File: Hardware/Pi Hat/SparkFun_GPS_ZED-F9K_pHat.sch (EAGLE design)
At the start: 67 parts, among them J1 QWIIC_RIGHT_ANGLE, J2 RASPBERRYPI-40-PIN-GPIO_SMD_S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, J4 U.FL, U1 UBLOX_ZED_F9R

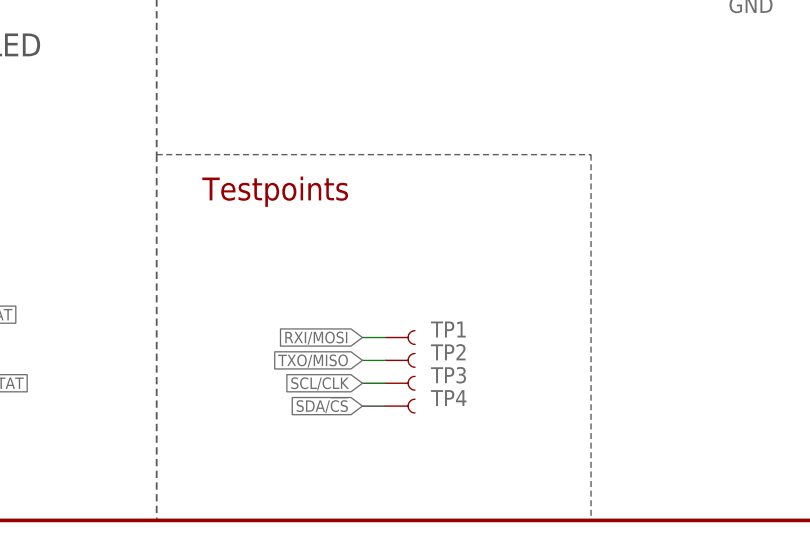
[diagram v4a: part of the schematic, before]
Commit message: Adds test point for power
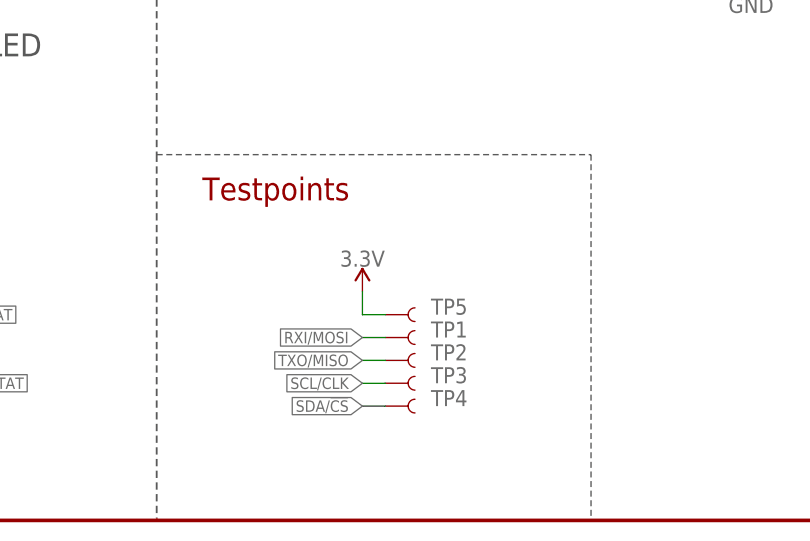
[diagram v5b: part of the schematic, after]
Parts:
- added TP5: TEST-POINT3X4, SparkFun-Connectors:TEST-POINT3X4
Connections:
- net 3.3V: now also TP5.1
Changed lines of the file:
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@@
 <part name="TP3" library="SparkFun-Connectors" deviceset="TEST-POINT" device="3X4" value="TEST-POINT3X4"/>
 <part name="TP4" library="SparkFun-Connectors" deviceset="TEST-POINT" device="3X4" value="TEST-POINT3X4"/>
+<part name="TP5" library="SparkFun-Connectors" deviceset="TEST-POINT" device="3X4" value="TEST-POINT3X4"/>
+<part name="SUPPLY8" library="SparkFun-PowerSymbols" deviceset="3.3V" device=""/>
 </parts>
 <sheets>
@@
 <attribute name="NAME" x="276.86" y="12.7" size="1.778" layer="95" font="vector"/>
 </instance>
+<instance part="TP5" gate="G$1" x="271.78" y="22.86" smashed="yes">
+<attribute name="NAME" x="276.86" y="22.86" size="1.778" layer="95" font="vector"/>
+</instance>
+<instance part="SUPPLY8" gate="G$1" x="269.24" y="25.4" smashed="yes">
+<attribute name="VALUE" x="269.24" y="28.194" size="1.778" layer="96" align="bottom-center"/>
+</instance>
 </instances>
 <busses>
@@
 <pinref part="SUPPLY4" gate="G$1" pin="3.3V"/>
 </segment>
+<segment>
+<pinref part="TP5" gate="G$1" pin="1"/>
+<wire x1="271.78" y1="22.86" x2="269.24" y2="22.86" width="0.1524" layer="91"/>
+<wire x1="269.24" y1="22.86" x2="269.24" y2="25.4" width="0.1524" layer="91"/>
+<pinref part="SUPPLY8" gate="G$1" pin="3.3V"/>
+</segment>
 </net>
 <net name="SCL/CLK" class="0">
@@
 </segment>
 </net>
-<net name="RF_IN" class="0">
+<net name="RF_IN" class="1">
 <segment>
 <label x="134.62" y="81.28" size="1.27" layer="95" xref="yes"/>

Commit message: Adds wheel tick and direction circuit to pi-hat
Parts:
- added C2, C5: 1.0nF, SparkFun-Capacitors:1.0NF/1000PF-0402_TIGHT-50V-10%
- added C3, C4: 22nF, SparkFun-Capacitors:22NF/22,000PF-0603-50V-10%
- added C7, C8, C9: 0.1uF, SparkFun-Capacitors:0.1UF-0402-16V-10%
- added D7, D8: 0.5A/40V/420mV, SparkFun-DiscreteSemi:DIODE-SCHOTTKY-PMEG4005EJ
- added R21, R31: 3.3k, SparkFun-Resistors:3.3KOHM-0603-1/10W-1%
- added R30, R32: 470, SparkFun-Resistors:470OHM-0603-1/10W-1%
- added R33, R34: 910, classified:910OHM-0603-1/10W-5%
- added U$30, U$31: UHS_INVERTER_SCHMITT_TRIGGERSIP6, classified:UHS_INVERTER_SCHMITT_TRIGGERSIP6
- added U2: HCPL-270L, classified:HCPL-270L
- J3: device SparkFun-Connectors:CONN_07NO_SILK -> SparkFun-Connectors:CONN_09NO_SILK
- J8: device SparkFun-Connectors:USB_C2-LAYER -> SparkFun-Connectors:USB_C_2-LAYER
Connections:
- removed net DIR: J3.7, R29.1
- removed net WT: J3.6, R28.1
- new net DIR+: J3.8, R31.1
- new net DIR-: C2.2, D8.A, J3.9, U2.CATHODE2
- new net DIR_IN: R32.2, U2.ANODE2
- new net DIR_OUT: R29.1, U$31.Y
- new net DIR_SCHMITT: C4.1, R34.1, U$31.A, U2.VOUT2
- new net N$27: C5.1, D7.C, R21.2, R30.1
- new net N$36: C2.1, D8.C, R31.2, R32.1
- new net WT+: J3.6, R21.1
- new net WT-: C5.2, D7.A, J3.7, U2.CATHODE1
- new net WT_IN: R30.2, U2.ANODE1
- new net WT_OUT: R28.1, U$30.Y
- new net WT_SCHMITT: C3.1, R33.1, U$30.A, U2.VOUT1
- net 3.3V: now also C7.1, C8.1, C9.1, R33.2, R34.2, U$30.VCC, U$31.VCC, U2.VCC
- net GND: now also C3.2, C4.2, C7.2, C8.2, C9.2, U$30.GND, U$31.GND, U2.GND
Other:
- moved on the sheet: C6, R12

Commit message: Routes wheel tick and direction circuitry
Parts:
- added TP6, TP7: TEST-POINT3X4, SparkFun-Connectors:TEST-POINT3X4
- C2, C5: device SparkFun-Capacitors:1.0NF/1000PF-0402_TIGHT-50V-10% -> SparkFun-Capacitors:1.0NF/1000PF-0402-50V-10%
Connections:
- net DIR_OUT: now also TP7.1
- net WT_OUT: now also TP6.1
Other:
- note added: "Wheel Tick and Direction Circuitry"
- moved on the sheet: B1, C1, C2, C3, C4, C5, C7, C8, C9, D1, D2, D3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

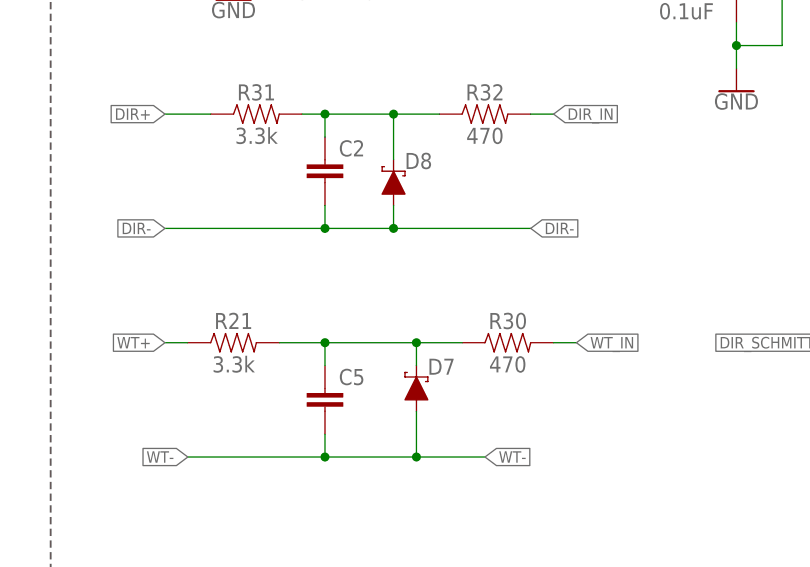
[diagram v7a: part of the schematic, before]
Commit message: Adds automotive certified diode to wt/dir circuitry
* Adds wt/dir circuitry to both breakout board and pi hat
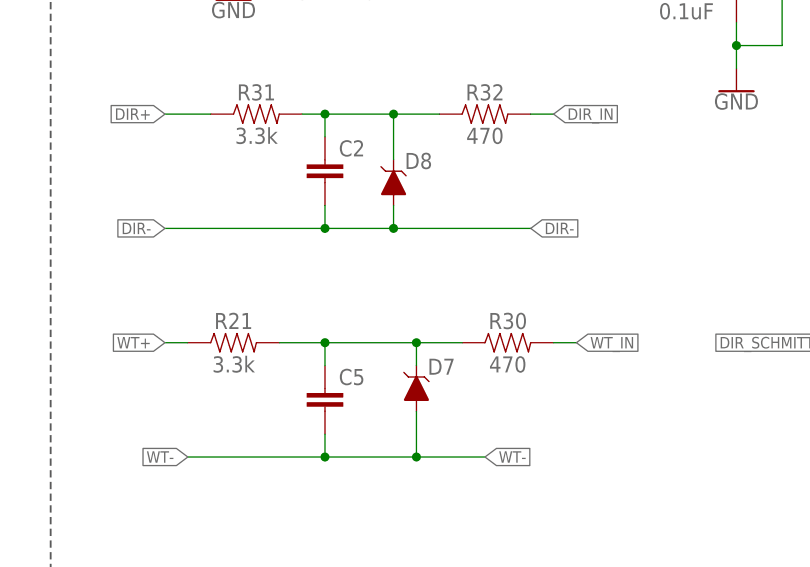
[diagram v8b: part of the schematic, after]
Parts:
- D7, D8: device SparkFun-DiscreteSemi:DIODE-SCHOTTKY-PMEG4005EJ -> classified:BZX84_DIODE
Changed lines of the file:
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@@
 <part name="C4" library="SparkFun-Capacitors" deviceset="22NF/22,000PF" device="-0603-50V-10%" value="22nF"/>
 <part name="C5" library="SparkFun-Capacitors" deviceset="1.0NF/1000PF" device="-0402-50V-10%" value="1.0nF"/>
-<part name="D7" library="SparkFun-DiscreteSemi" deviceset="DIODE-SCHOTTKY" device="-PMEG4005EJ" value="0.5A/40V/420mV"/>
+<part name="D7" library="classified" deviceset="BZX84_DIODE" device="" value="0.5A/40V/420mV"/>
 <part name="R33" library="classified" deviceset="910OHM-0603-1/10W-5%" device="" value="910"/>
 <part name="R34" library="classified" deviceset="910OHM-0603-1/10W-5%" device="" value="910"/>
@@
 <part name="SUPPLY10" library="SparkFun-PowerSymbols" deviceset="3.3V" device=""/>
 <part name="GND12" library="SparkFun-PowerSymbols" deviceset="GND" device=""/>
-<part name="D8" library="SparkFun-DiscreteSemi" deviceset="DIODE-SCHOTTKY" device="-PMEG4005EJ" value="0.5A/40V/420mV"/>
+<part name="D8" library="classified" deviceset="BZX84_DIODE" device="" value="0.5A/40V/420mV"/>
 <part name="GND13" library="SparkFun-PowerSymbols" deviceset="GND" device=""/>
 <part name="GND14" library="SparkFun-PowerSymbols" deviceset="GND" device=""/>
